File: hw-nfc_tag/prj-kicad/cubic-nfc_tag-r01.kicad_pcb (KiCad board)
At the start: 2 copper layers, 40 x 40 mm, 13 parts, among them P1 CONN_1, P2 CONN_1, P3 CONN_1, P4 CONN_1, P5 CONN_1, P6 CONN_1, P7 CONN_1, P8 CONN_1, P9 CONN_1, U1 M24LR04E

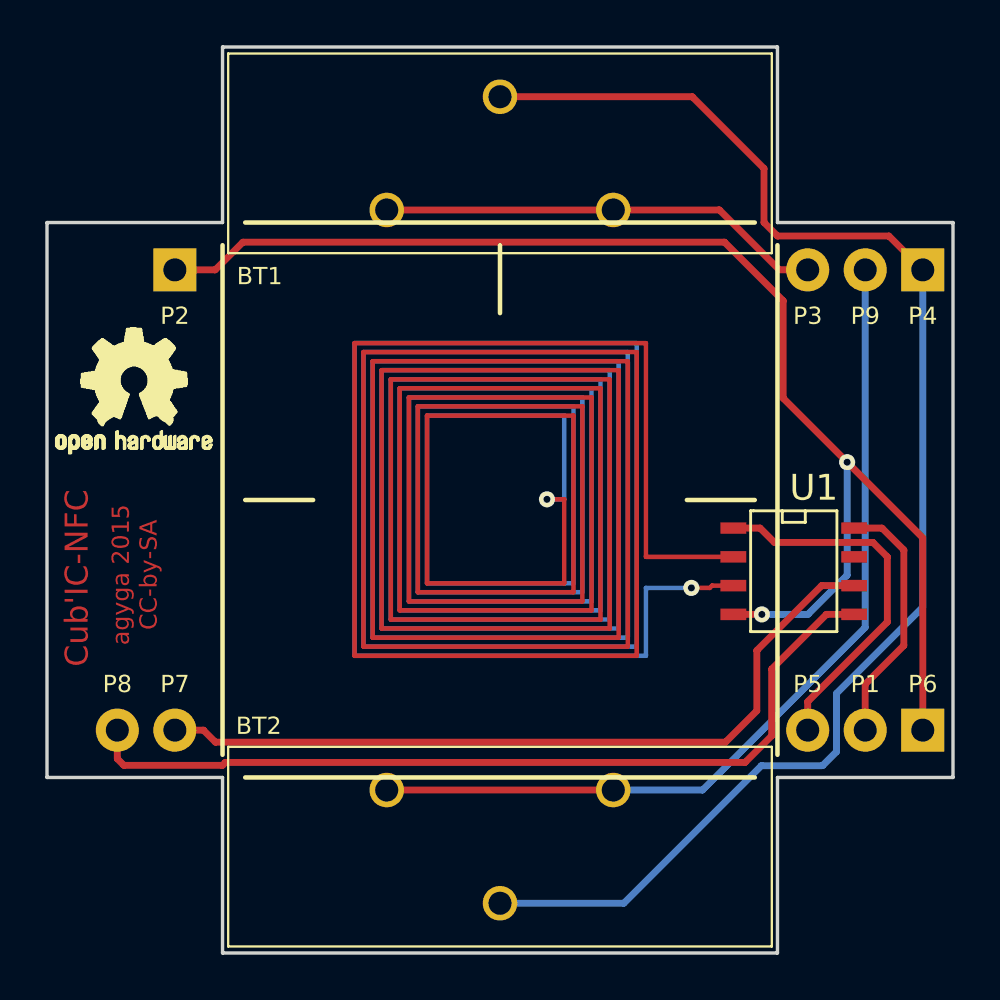
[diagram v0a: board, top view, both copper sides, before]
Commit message: = UPD: Move ground pad and add a second communication port
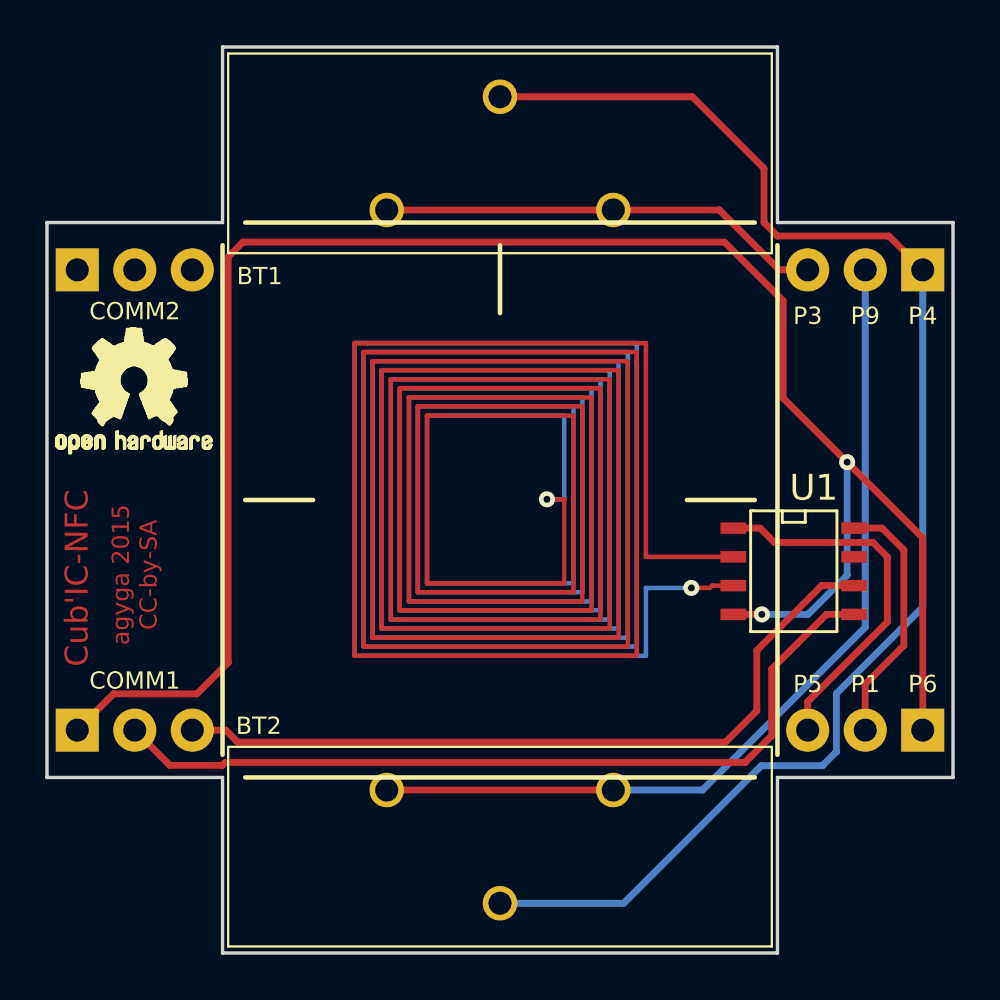
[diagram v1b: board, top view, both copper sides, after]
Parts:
- removed P2: CONN_1, TP_PIN_C
- removed P7, P8: CONN_1, TP_PIN
- added COMM1: CONN_3, CONN_3, F.Cu at (146.1, 97.4)
- added COMM2: CONN_3, CONN_3, F.Cu at (146.1, 77.1)
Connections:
- U1 pad 5: N-000001 (its old number) -> I2C_SDA
- U1 pad 6: N-000004 -> I2C_SCL
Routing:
- net N-000001 (its old number): track 38.4 -> 0.00 mm
- net I2C_SDA: track 0.00 -> 36.9 mm
- net N-000004: track 34.6 -> 0.00 mm
- net I2C_SCL: track 0.00 -> 33.9 mm
- net GND: track 60.7 -> 83.9 mm
